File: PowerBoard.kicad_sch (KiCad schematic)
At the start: 15 parts, among them J101 Conn_01x04_Pin, J102 Conn_01x04_Pin, J103 Conn_01x04_Pin, J104 Conn_01x04_Pin, J105 Conn_01x02_Pin, J106 Conn_01x02_Pin, J107 Conn_01x02_Pin, J108 Conn_01x06_Pin, J109 Conn_01x06_Pin, J110 USB_C_Receptacle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

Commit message: Big Moves
Big Moves
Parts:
- U101: footprint MCU_Teensy:Teensy_4.1 -> MCU_Teensy:Teensy41_bare_pins
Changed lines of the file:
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@@
     (pin "6")
     (instances
-      (project "power"
+      (project "PowerBoard"
         (path "/0d766aee-3212-42a6-9533-08f4b759e61c"
           (reference "J108") (unit 1)
@@
       (effects (font (size 1.27 1.27)))
     )
-    (property "Footprint" "MCU_Teensy:Teensy_4.1" (at 68.453 128.905 0)
+    (property "Footprint" "MCU_Teensy:Teensy41_bare_pins" (at 68.453 128.905 0)
       (effects (font (size 1.27 1.27)) hide)
     )
@@
     (pin "4")
     (instances
-      (project "power"
+      (project "PowerBoard"
         (path "/0d766aee-3212-42a6-9533-08f4b759e61c"
           (reference "U101") (unit 1)
@@
     (pin "1")
     (instances
-      (project "power"
+      (project "PowerBoard"
         (path "/0d766aee-3212-42a6-9533-08f4b759e61c"
           (reference "#PWR0115") (unit 1)
@@
     (pin "2")
     (instances
-      (project "power"
+      (project "PowerBoard"
         (path "/0d766aee-3212-42a6-9533-08f4b759e61c"
           (reference "J105") (unit 1)
@@
     (pin "1")
     (instances
-      (project "power"
+      (project "PowerBoard"
         (path "/0d766aee-3212-42a6-9533-08f4b759e61c"
           (reference "#PWR0101") (unit 1)
@@
     (pin "6")
     (instances
-      (project "power"
+      (project "PowerBoard"
         (path "/0d766aee-3212-42a6-9533-08f4b759e61c"
           (reference "J109") (unit 1)
@@
     (pin "1")
     (instances
-      (project "power"
+      (project "PowerBoard"
         (path "/0d766aee-3212-42a6-9533-08f4b759e61c"
           (reference "#PWR0111") (unit 1)
@@
     (pin "1")
     (instances
-      (project "power"
+      (project "PowerBoard"
         (path "/0d766aee-3212-42a6-9533-08f4b759e61c"
           (reference "#PWR0112") (unit 1)
@@
     (pin "1")
     (instances
-      (project "power"
+      (project "PowerBoard"
         (path "/0d766aee-3212-42a6-9533-08f4b759e61c"
           (reference "#PWR0113") (unit 1)
@@
     (pin "4")
     (instances
-      (project "power"
+      (project "PowerBoard"
         (path "/0d766aee-3212-42a6-9533-08f4b759e61c"
           (reference "J101") (unit 1)
@@
     (pin "1")
     (instances
-      (project "power"
+      (project "PowerBoard"
         (path "/0d766aee-3212-42a6-9533-08f4b759e61c"
           (reference "#PWR0114") (unit 1)
@@
     (pin "2")
     (instances
-      (project "power"
+      (project "PowerBoard"
         (path "/0d766aee-3212-42a6-9533-08f4b759e61c"
           (reference "J106") (unit 1)
@@
     (pin "1")
     (instances
-      (project "power"
+      (project "PowerBoard"
         (path "/0d766aee-3212-42a6-9533-08f4b759e61c"
           (reference "#PWR0110") (unit 1)
@@
     (pin "1")
     (instances
-      (project "power"
+      (project "PowerBoard"
         (path "/0d766aee-3212-42a6-9533-08f4b759e61c"
           (reference "#PWR0109") (unit 1)
@@
     (pin "4")
     (instances
-      (project "power"
+      (project "PowerBoard"
         (path "/0d766aee-3212-42a6-9533-08f4b759e61c"
           (reference "J104") (unit 1)
@@
     (pin "1")
     (instances
-      (project "power"
+      (project "PowerBoard"
         (path "/0d766aee-3212-42a6-9533-08f4b759e61c"
           (reference "#PWR0108") (unit 1)
@@
     (pin "1")
     (instances
-      (project "power"
+      (project "PowerBoard"
         (path "/0d766aee-3212-42a6-9533-08f4b759e61c"
           (reference "#PWR0106") (unit 1)
@@
     (pin "1")
     (instances
-      (project "power"
+      (project "PowerBoard"
         (path "/0d766aee-3212-42a6-9533-08f4b759e61c"
           (reference "#PWR0104") (unit 1)
@@
     (pin "1")
     (instances
-      (project "power"
+      (project "PowerBoard"
         (path "/0d766aee-3212-42a6-9533-08f4b759e61c"
           (reference "#PWR0107") (unit 1)
@@
     (pin "1")
     (instances
-      (project "power"
+      (project "PowerBoard"
         (path "/0d766aee-3212-42a6-9533-08f4b759e61c"
           (reference "#PWR0117") (unit 1)
@@
     (pin "9")
     (instances
-      (project "power"
+      (project "PowerBoard"
         (path "/0d766aee-3212-42a6-9533-08f4b759e61c"
           (reference "U104") (unit 1)
@@
     (pin "1")
     (instances
-      (project "power"
+      (project "PowerBoard"
         (path "/0d766aee-3212-42a6-9533-08f4b759e61c"
           (reference "#PWR0116") (unit 1)
@@
     (pin "5")
     (instances
-      (project "power"
+      (project "PowerBoard"
         (path "/0d766aee-3212-42a6-9533-08f4b759e61c"
           (reference "U103") (unit 1)
@@
     (pin "S1")
     (instances
-      (project "power"
+      (project "PowerBoard"
         (path "/0d766aee-3212-42a6-9533-08f4b759e61c"
           (reference "J110") (unit 1)
@@
     (pin "2")
     (instances
-      (project "power"
+      (project "PowerBoard"
         (path "/0d766aee-3212-42a6-9533-08f4b759e61c"
           (reference "R104") (unit 1)
@@
     (pin "1")
     (instances
-      (project "power"
+      (project "PowerBoard"
         (path "/0d766aee-3212-42a6-9533-08f4b759e61c"
           (reference "#PWR0102") (unit 1)
@@
     (pin "4")
     (instances
-      (project "power"
+      (project "PowerBoard"
         (path "/0d766aee-3212-42a6-9533-08f4b759e61c"
           (reference "J102") (unit 1)
@@
     (pin "4")
     (instances
-      (project "power"
+      (project "PowerBoard"
         (path "/0d766aee-3212-42a6-9533-08f4b759e61c"
           (reference "J103") (unit 1)
@@
     (pin "1")
     (instances
-      (project "power"
+      (project "PowerBoard"
         (path "/0d766aee-3212-42a6-9533-08f4b759e61c"
           (reference "#PWR0118") (unit 1)
@@
     (pin "2")
     (instances
-      (project "power"
+      (project "PowerBoard"
         (path "/0d766aee-3212-42a6-9533-08f4b759e61c"
           (reference "J107") (unit 1)
@@
     (pin "1")
     (instances
-      (project "power"
+      (project "PowerBoard"
         (path "/0d766aee-3212-42a6-9533-08f4b759e61c"
           (reference "#PWR0105") (unit 1)
@@
     (pin "2")
     (instances
-      (project "power"
+      (project "PowerBoard"
         (path "/0d766aee-3212-42a6-9533-08f4b759e61c"
           (reference "D101") (unit 1)

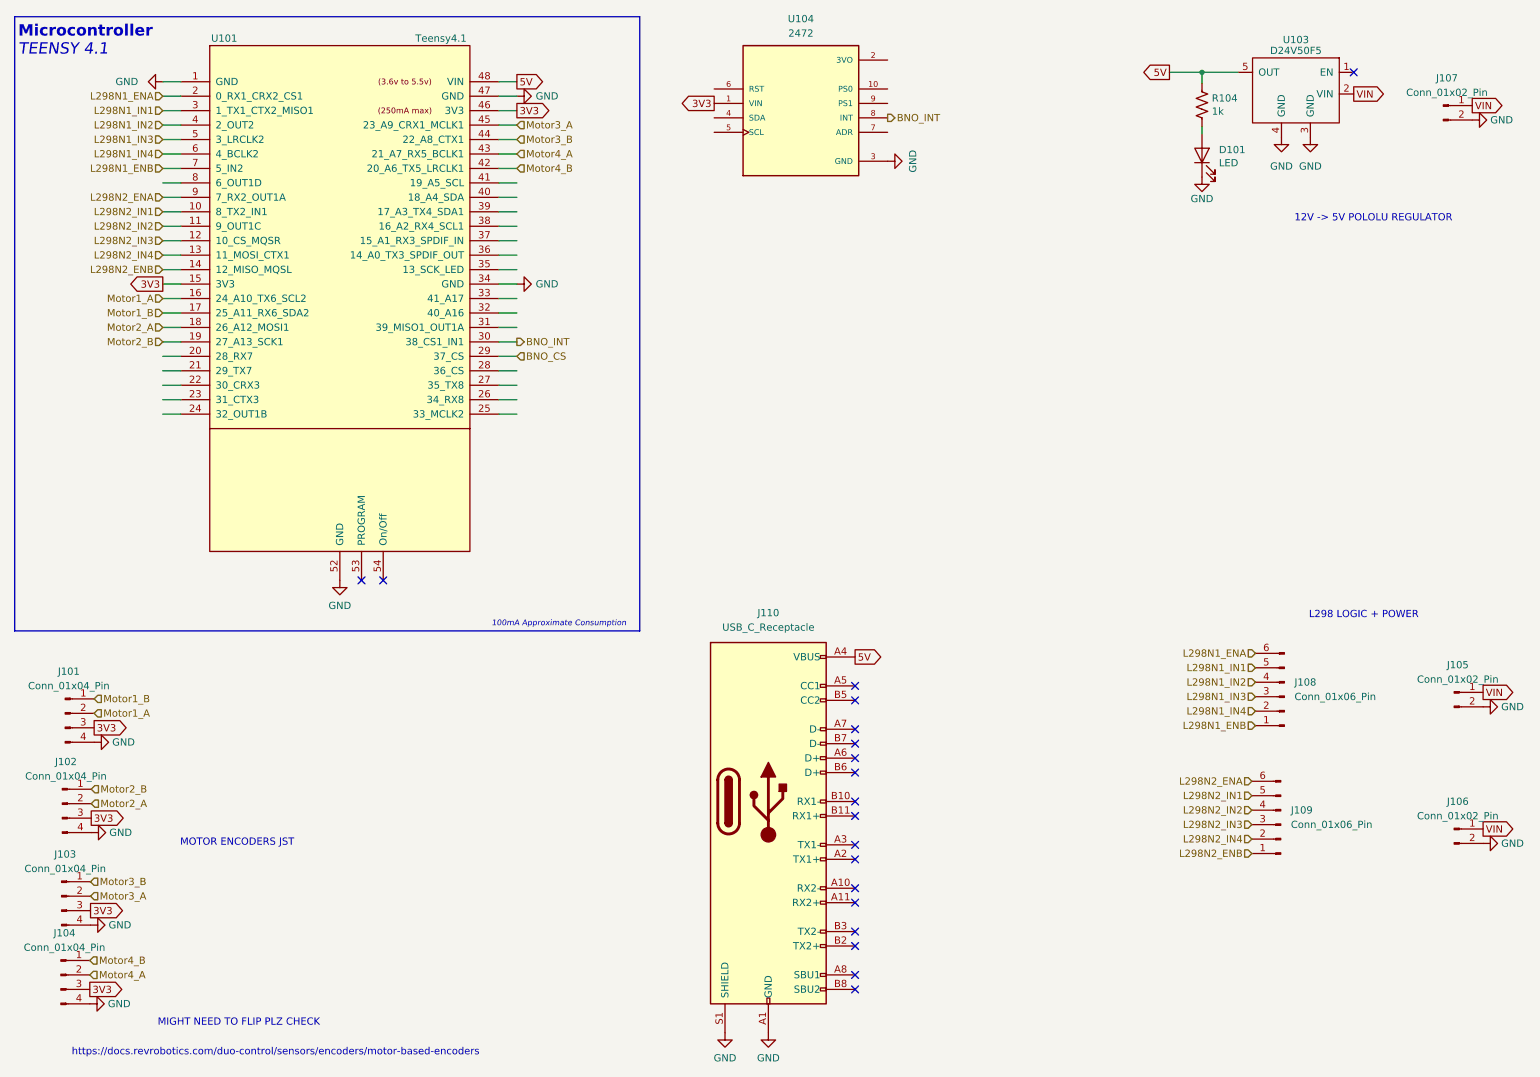
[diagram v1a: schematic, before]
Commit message: ready for review
Flipped encoder connector pinout, added mounting holes, fixed battery connector footprint, moved USB C connector, added memes, added placeholder names
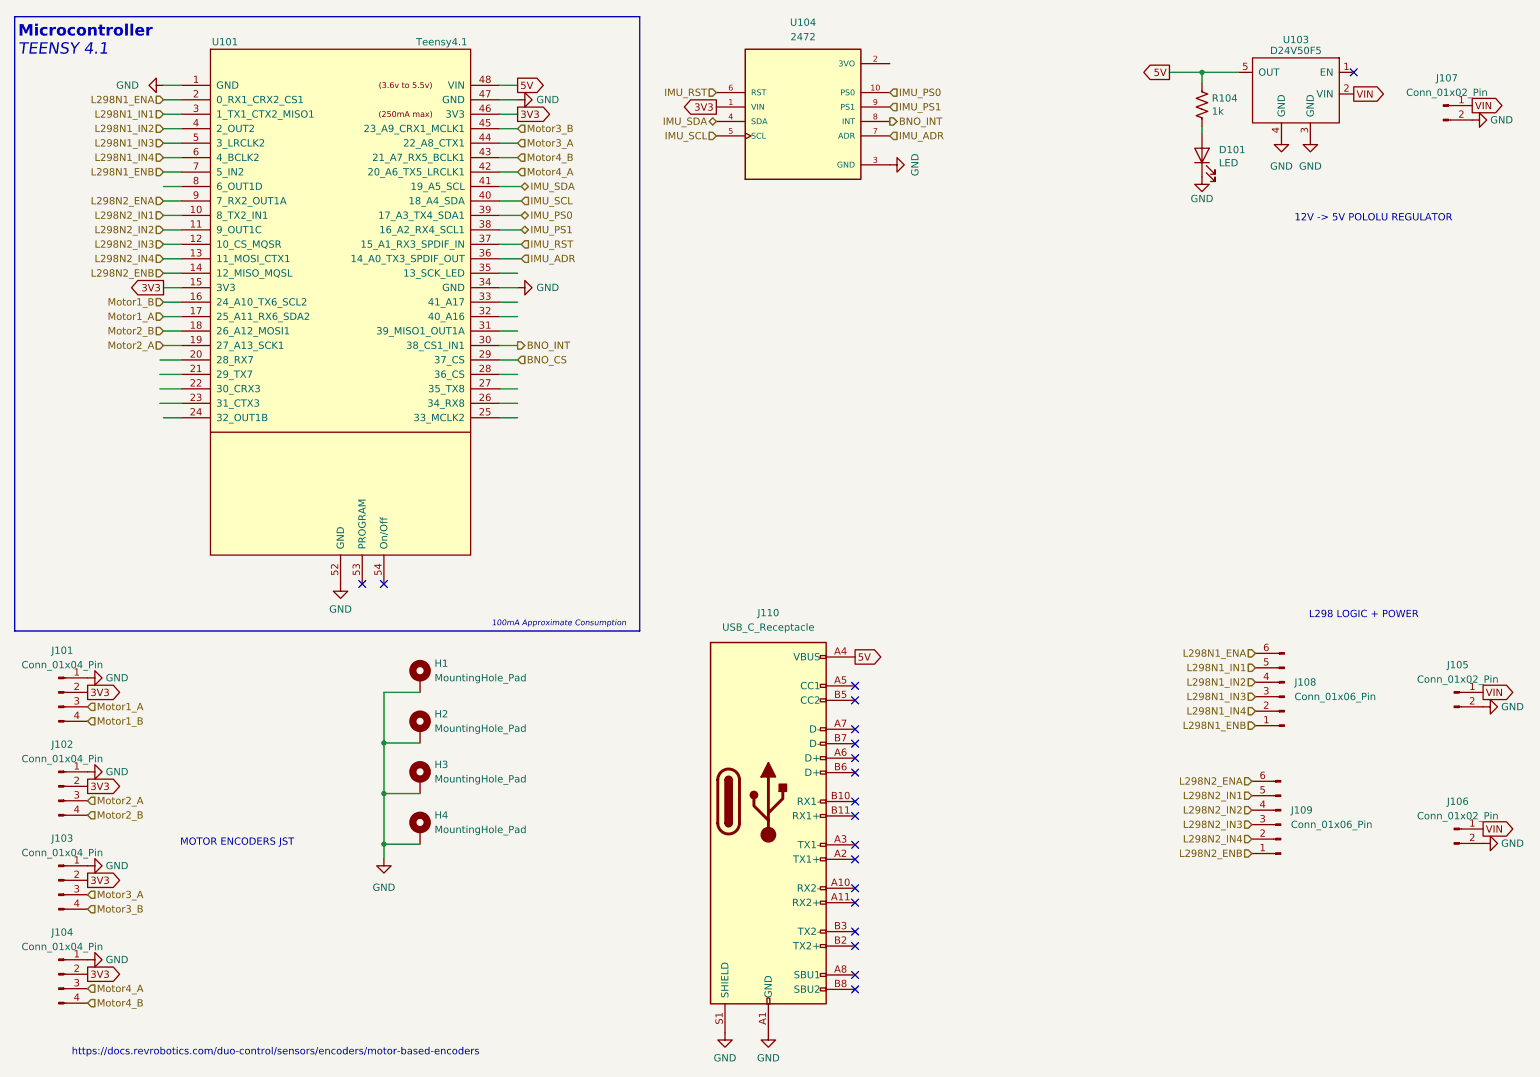
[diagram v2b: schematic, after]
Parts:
- added H1, H2, H3, H4: MountingHole_Pad, MountingHole:MountingHole_3.2mm_M3_Pad_Via, symbol Mechanical:MountingHole_Pad
- J107: footprint Connector_AMASS:AMASS_XT60-F_1x02_P7.20mm_Vertical -> Connector_AMASS:AMASS_XT60-M_1x02_P7.20mm_Vertical
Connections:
- net 3V3: now also J101.2 (Pin_2), J102.2 (Pin_2), J103.2 (Pin_2), J104.2 (Pin_2); no longer J101.3 (Pin_3), J102.3 (Pin_3), J103.3 (Pin_3), J104.3 (Pin_3)
- net GND: now also J101.1 (Pin_1), J102.1 (Pin_1), J103.1 (Pin_1), J104.1 (Pin_1), H1.1, H2.1, H3.1, H4.1; no longer J101.4 (Pin_4), J102.4 (Pin_4), J103.4 (Pin_4), J104.4 (Pin_4)
- net Motor1_A: now also J101.3 (Pin_3), U101.17 (25_A11_RX6_SDA2); no longer J101.2 (Pin_2), U101.16 (24_A10_TX6_SCL2)
- net Motor1_B: now also J101.4 (Pin_4), U101.16 (24_A10_TX6_SCL2); no longer J101.1 (Pin_1), U101.17 (25_A11_RX6_SDA2)
- net Motor2_A: now also J102.3 (Pin_3), U101.19 (27_A13_SCK1); no longer J102.2 (Pin_2), U101.18 (26_A12_MOSI1)
- net Motor2_B: now also J102.4 (Pin_4), U101.18 (26_A12_MOSI1); no longer J102.1 (Pin_1), U101.19 (27_A13_SCK1)
- net Motor3_A: now also J103.3 (Pin_3), U101.44 (22_A8_CTX1); no longer J103.2 (Pin_2), U101.45 (23_A9_CRX1_MCLK1)
- net Motor3_B: now also J103.4 (Pin_4), U101.45 (23_A9_CRX1_MCLK1); no longer J103.1 (Pin_1), U101.44 (22_A8_CTX1)
- net Motor4_A: now also J104.3 (Pin_3), U101.42 (20_A6_TX5_LRCLK1); no longer J104.2 (Pin_2), U101.43 (21_A7_RX5_BCLK1)
- net Motor4_B: now also J104.4 (Pin_4), U101.43 (21_A7_RX5_BCLK1); no longer J104.1 (Pin_1), U101.42 (20_A6_TX5_LRCLK1)
- net IMU_ADR: now reaches U101.36 (14_A0_TX3_SPDIF_OUT)
- net IMU_ADR: now also U104.7 (ADR)
- net IMU_RST: now reaches U101.37 (15_A1_RX3_SPDIF_IN)
- net IMU_RST: now also U104.6 (RST)
- net IMU_PS1: now reaches U101.38 (16_A2_RX4_SCL1)
- net IMU_PS1: now also U104.9 (PS1)
- net IMU_PS0: now reaches U101.39 (17_A3_TX4_SDA1)
- net IMU_PS0: now also U104.10 (PS0)
- net IMU_SCL: now reaches U101.40 (18_A4_SDA)
- net IMU_SCL: now also U104.5 (SCL)
- net IMU_SDA: now reaches U101.41 (19_A5_SCL)
- net IMU_SDA: now also U104.4 (SDA)
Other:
- note removed: "MIGHT NEED TO FLIP PLZ CHECK"
- moved on the sheet: J101, J102, J103, U101, U104

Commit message: only need names
should be ready to order the board once we get list of names for back silkscreen
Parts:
- removed H4: MountingHole_Pad, MountingHole:MountingHole_3.2mm_M3_Pad_Via, symbol Mechanical:MountingHole_Pad
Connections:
- net IMU_SCL: now also U101.41 (19_A5_SCL); no longer U101.40 (18_A4_SDA)
- net IMU_SDA: now also U101.40 (18_A4_SDA); no longer U101.41 (19_A5_SCL)
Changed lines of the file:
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@@
 (kicad_sch (version 20230121) (generator eeschema)
   (paper "A4")
-  (junction (at 78.74 158.75) (diameter 0) (color 0 0 0 0)
-  )
   (junction (at 78.74 149.86) (diameter 0) (color 0 0 0 0)
   )
@@
     (stroke (width 0) (type default))
   )
-  (wire (pts (xy 78.74 158.75) (xy 78.74 161.29))
+  (wire (pts (xy 78.74 149.86) (xy 78.74 156.21))
     (stroke (width 0) (type default))
   )
@@
     (stroke (width 0) (type default))
   )
-  (wire (pts (xy 78.74 158.75) (xy 85.09 158.75))
-    (stroke (width 0) (type default))
-  )
   (wire (pts (xy 222.504 25.019) (xy 222.504 23.114))
-    (stroke (width 0) (type default))
-  )
-  (wire (pts (xy 78.74 149.86) (xy 78.74 158.75))
     (stroke (width 0) (type default))
   )
@@
     (effects (font (size 1.27 1.27)) (justify left))
   )
-  (hierarchical_label "IMU_PS1" (shape bidirectional) (at 102.87 50.8 0) (fields_autoplaced)
+  (hierarchical_label "IMU_PS1" (shape output) (at 102.87 50.8 0) (fields_autoplaced)
     (effects (font (size 1.27 1.27)) (justify left))
   )
@@
     (effects (font (size 1.27 1.27)) (justify right))
   )
-  (hierarchical_label "IMU_PS0" (shape bidirectional) (at 102.87 48.26 0) (fields_autoplaced)
+  (hierarchical_label "IMU_PS0" (shape output) (at 102.87 48.26 0) (fields_autoplaced)
     (effects (font (size 1.27 1.27)) (justify left))
   )
@@
     (effects (font (size 1.27 1.27)) (justify right))
   )
-  (hierarchical_label "IMU_SDA" (shape bidirectional) (at 102.87 43.18 0) (fields_autoplaced)
+  (hierarchical_label "IMU_SDA" (shape bidirectional) (at 102.87 45.72 0) (fields_autoplaced)
     (effects (font (size 1.27 1.27)) (justify left))
   )
@@
     (effects (font (size 1.27 1.27)) (justify right))
   )
-  (hierarchical_label "IMU_SCL" (shape input) (at 102.87 45.72 0) (fields_autoplaced)
+  (hierarchical_label "IMU_SCL" (shape input) (at 102.87 43.18 0) (fields_autoplaced)
     (effects (font (size 1.27 1.27)) (justify left))
   )
@@
     )
   )
-  (symbol (lib_name "GND_2") (lib_id "power:GND") (at 78.74 161.29 0) (mirror y) (unit 1)
-    (in_bom yes) (on_board yes) (dnp no) (fields_autoplaced)
-    (property "Reference" "#PWR01" (at 78.74 167.64 0)
-      (effects (font (size 1.27 1.27)) hide)
-    )
-    (property "Value" "GND" (at 78.74 166.37 0)
-      (effects (font (size 1.27 1.27)))
-    )
-    (property "Footprint" "" (at 78.74 161.29 0)
-      (effects (font (size 1.27 1.27)) hide)
-    )
-    (property "Datasheet" "" (at 78.74 161.29 0)
+  (symbol (lib_name "GND_2") (lib_id "power:GND") (at 78.74 156.21 0) (mirror y) (unit 1)
+    (in_bom yes) (on_board yes) (dnp no) (fields_autoplaced)
+    (property "Reference" "#PWR01" (at 78.74 162.56 0)
+      (effects (font (size 1.27 1.27)) hide)
+    )
+    (property "Value" "GND" (at 78.74 161.29 0)
+      (effects (font (size 1.27 1.27)))
+    )
+    (property "Footprint" "" (at 78.74 156.21 0)
+      (effects (font (size 1.27 1.27)) hide)
+    )
+    (property "Datasheet" "" (at 78.74 156.21 0)
       (effects (font (size 1.27 1.27)) hide)
     )
@@
         )
       )
-    )
-  )
-  (symbol (lib_id "Mechanical:MountingHole_Pad") (at 85.09 156.21 0) (unit 1)
-    (in_bom yes) (on_board yes) (dnp no) (fields_autoplaced)
-    (property "Reference" "H4" (at 87.63 153.67 0)
-      (effects (font (size 1.27 1.27)) (justify left))
-    )
-    (property "Value" "MountingHole_Pad" (at 87.63 156.21 0)
-      (effects (font (size 1.27 1.27)) (justify left))
-    )
-    (property "Footprint" "MountingHole:MountingHole_3.2mm_M3_Pad_Via" (at 85.09 156.21 0)
-      (effects (font (size 1.27 1.27)) hide)
-    )
-    (property "Datasheet" "~" (at 85.09 156.21 0)
-      (effects (font (size 1.27 1.27)) hide)
-    )
-    (pin "1")
-    (instances
-      (project "PowerBoard"
-        (path "/0d766aee-3212-42a6-9533-08f4b759e61c"
-          (reference "H4") (unit 1)
-        )
-      )
